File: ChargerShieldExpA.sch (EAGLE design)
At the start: 99 parts, among them IC1 LM324N, IC2 TL431, Q1 BD648, Q2 BUZ11, Q3 BUZ171, Q4 IRFZ48Z, T2 BC548, X1 +Vin, X2 Battery, X3 VCC

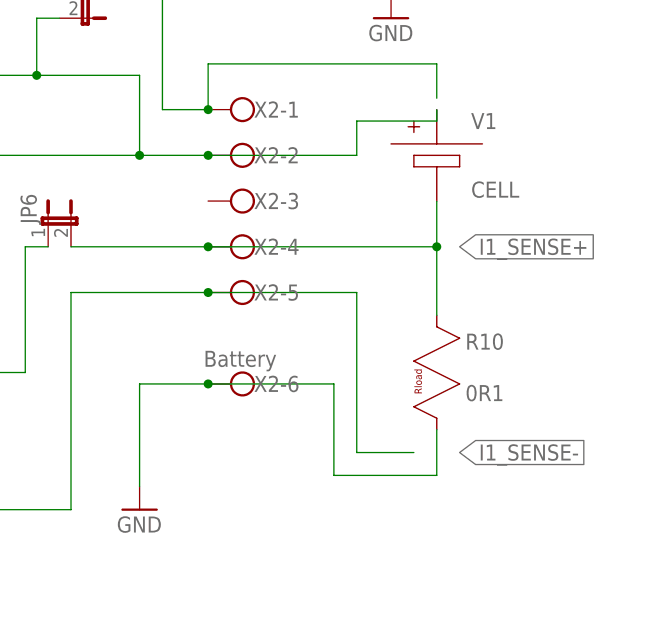
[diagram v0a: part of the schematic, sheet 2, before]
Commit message: internal current sense shunt
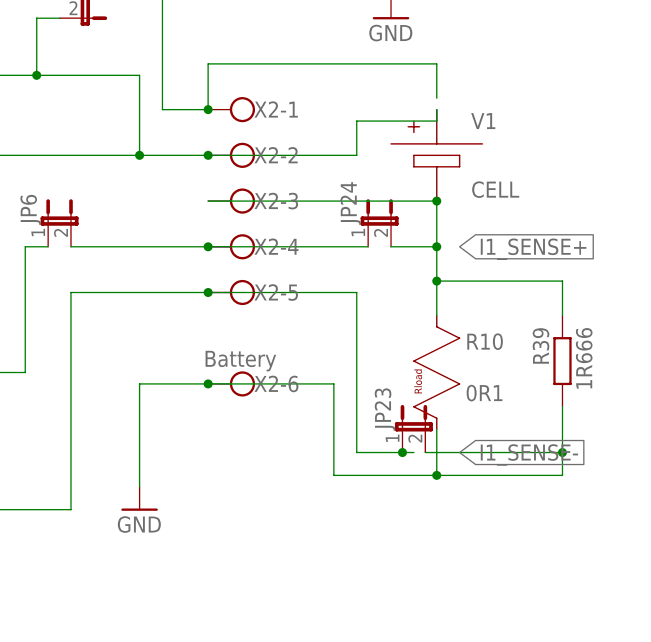
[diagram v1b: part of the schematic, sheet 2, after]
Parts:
- added JP23, JP24: (no value), bigger:JP1E
- added R39: 1R666, rcl:R-EU_0414/15
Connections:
- new net N$54: JP24.1, JP6.2, X2-4.KL
- net GND: now also JP23.2, R39.2
- net I1_SENSE+: now also JP24.2, R39.1, X2-3.KL; no longer JP6.2, X2-4.KL
- net I1_SENSE-: now also JP23.1

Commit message: renumbered
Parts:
- removed C8: 100n, rcl:C-EU025_050-025X075
- removed R39: 1R666, rcl:R-EU_0414/15
- added C7: 10µ, rcl:CPOL-EUE5-5
- added RA10: 0R1, lt-spice-simulation:RES_RLOAD
- C1, C6: value 10µ -> 100n; device rcl:CPOL-EUE5-5 -> rcl:C-EU025_050-025X075
- C4: value 100n -> 3µ3; device rcl:C-EU025_050-025X075 -> rcl:CPOL-EUE5-5
- C5: value 3µ3 -> 10µ
- IC1: value LM324N -> TL431; device linear:LM324N -> AWJLEagleLib:TL431TO92
- IC2: value TL431 -> LM324N; device AWJLEagleLib:TL431TO92 -> linear:LM324N
- JP1, JP2, JP6, JP8: device bigger:JP1E -> bigger:JP2E
- JP16, JP17, JP18, JP9: device bigger:JP2E -> bigger:JP1E
- LED2: value (none) -> CHRG2
- LED3: value CHRG2 -> (none)
- Q1: value BD648 -> BUZ11; device transistor-pnp:BD648 -> transistor-fet:BUZ11
- Q2: value BUZ11 -> BD648; device transistor-fet:BUZ11 -> transistor-pnp:BD648
- R1: value 470 -> 4k7; device rcl:R-EU_0207/12 -> rcl:R-EU_0204/7
- R10: value 0R1 -> 2k2; device lt-spice-simulation:RES_RLOAD -> rcl:R-EU_0207/15
- R11: value 100k -> 1k; device rcl:R-EU_0207/10 -> rcl:R-EU_0204/7
- R12: value 1k -> 1R666; device rcl:R-EU_0207/12 -> rcl:R-EU_0414/15
- R14: value 10k -> 0
- R15: value 100k -> 1k
- R16: value 33k -> 1k
- R17: value 1k -> 12k; device rcl:R-EU_0207/15 -> rcl:R-EU_0207/10
- R18: value 12k -> 100k
- R19: value 1k -> 33k; device rcl:R-EU_0204/7 -> rcl:R-EU_0207/10
- R2: value 100k -> 4k7; device rcl:R-EU_0204/7 -> rcl:R-EU_0207/10
- R20: value 470 -> 1k; device rcl:R-EU_0207/10 -> rcl:R-EU_0207/15
- R21: value 200 -> 1k; device rcl:R-EU_0204/7 -> rcl:R-EU_0207/12
- R22: value 4k7 -> 200; device rcl:R-EU_0207/10 -> rcl:R-EU_0207/12
- R23: value 470 -> 1M
- R24: value 0 -> 100k; device rcl:R-EU_0207/10 -> rcl:R-EU_0204/7
- R25: value 4k7 -> 1k; device rcl:R-EU_0204/7 -> rcl:R-EU_0207/10
- R26: value 470 -> 100k
- R27: value 470 -> 10k; device rcl:R-EU_0204/7 -> rcl:R-EU_0207/10
- R28: value 0 -> 10k; device rcl:R-EU_0204/7 -> rcl:R-EU_0207/10
- R29: value 0 -> 1k; device rcl:R-EU_0204/7 -> rcl:R-EU_0207/12
- R3: device rcl:R-EU_0207/10 -> rcl:R-EU_0207/12
- R30: value 0 -> 100k; device rcl:R-EU_0204/7 -> rcl:R-EU_0207/10
- R31: value 0 -> 1R666; device rcl:R-EU_0204/7 -> rcl:R-EU_0414/15
- R33: device rcl:R-EU_0204/2V -> rcl:R-EU_0204/7
- R34: device rcl:R-EU_0204/7 -> rcl:R-EU_0204/2V
- R35: value 100k -> 0
- R36: value 1M -> 0; device rcl:R-EU_0207/10 -> rcl:R-EU_0204/7
- R37: value 200 -> 0; device rcl:R-EU_0207/12 -> rcl:R-EU_0204/7
- R38: value 1k -> 0; device rcl:R-EU_0207/10 -> rcl:R-EU_0204/7
- R4: value 2k2 -> 200; device rcl:R-EU_0207/15 -> rcl:R-EU_0204/7
- R5, R6: value 1k -> 470
- R7: value 1R666 -> 470; device rcl:R-EU_0414/15 -> rcl:R-EU_0207/10
- R8: value 1k -> 470; device rcl:R-EU_0207/12 -> rcl:R-EU_0204/7
- R9: value 10k -> 470; device rcl:R-EU_0207/10 -> rcl:R-EU_0204/7
- S4: value Discharge -> A
- S5: value A -> B
- S6: value B -> Discharge
- U$1: value ARDUINOR3BPLACE-LONG -> DS1820TO92; device arduino-long:ARDUINOR3BPLACE-LONG -> Ava:DS1820TO92
- U$2: value DS1820TO92 -> ARDUINOR3BPLACE-LONG; device Ava:DS1820TO92 -> arduino-long:ARDUINOR3BPLACE-LONG
- X2: value Battery -> VCC; device con-wago-500:W237-6 -> con-wago-500:W237-102
- X3: value VCC -> Battery; device con-wago-500:W237-102 -> con-wago-500:W237-6
- renumbered T2 to T1
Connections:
- net +5V: now also JP20.1, JP3.1, JP3.2, JP6.3, JP8.3, R1.2, R4.2, U$1.VCC, U$2.5V; no longer JP16.1, JP16.2, JP16.3, JP5.3, JP9.1, R21.2, R25.2, U$1.5V, U$2.VCC
- net GND: now also C1.2, C4.-, C7.-, IC1.A, IC2P.V-, JP17.2, JP2.1, JP2.2, JP2.3, JP20.3, JP4.2, JP6.1, R12.2, R17.1, R19.1, R23.1, R25.1, R26.1, R30.1, R31.2, R32.2, R33.2, R37.2, RA10.B, U$2.GND1, U$2.GND2, X2-2.KL, X3-6.KL; no longer C1.-, C4.2, C6.-, IC1P.V-, IC2.A, JP18.1, JP18.2, JP18.3, JP22.2, JP23.2, JP3.1, JP9.3, R10.B, R11.1, R16.1, R18.1, R28.2, R29.2, R34.2, R35.1, R36.1, R38.1, R39.2, R7.2, U$1.GND1, U$1.GND2, X2-6.KL, X3-2.KL
- net I1_SENSE+: now also JP16.2, R31.1, RA10.A, X3-3.KL; no longer JP24.2, R10.A, R39.1, X2-3.KL
- net I1_SENSE-: now also JP17.1, R28.1, X3-5.KL; no longer JP23.1, R9.1, X2-5.KL
- net I_BATT1: now also C4.+, R21.1, U$2.A1; no longer C2.+, R12.1, U$1.A1
- net I_BATT2: now also JP5.2, U$2.A4/SDA; no longer JP20.2, U$1.A4/SDA
- net I_DISC1: now also R20.2, U$2.A2; no longer R17.2, U$1.A2
- net I_DISC2: now also JP5.3, U$2.A5/SCL; no longer JP20.3, U$1.A5/SCL
- net N$1: now also R3.2, U$2.D13; no longer R1.2, U$1.D13
- net N$10: now also C6.1, JP13.1; no longer C8.1, JP1.1
- net N$11: now also IC2A.OUT, JP12.2, R24.2; no longer IC1A.OUT, JP7.2, R2.2
- net N$12: now also JP6.2, R1.1, U$1.DQ, U$2.D2; no longer JP3.2, R25.1, U$1.D2, U$2.DQ
- net N$13: now also JP13.2, JP15.2, Q1.D, X3-2.KL; no longer JP1.2, JP2.2, Q2.D, X2-2.KL
- net N$14: now also IC2A.-IN, R24.1, R28.2; no longer IC1A.-IN, R2.1, R9.2
- net N$15: now also IC2A.+IN, R26.2, R27.1; no longer IC1A.+IN, R14.1, R35.2
- net N$16: now also IC2B.-IN, R17.2, R18.1, R19.2; no longer IC1B.-IN, R15.1, R16.2, R18.2
- net N$17: now also IC2B.OUT, JP11.1, R18.2; no longer IC1B.OUT, JP15.1, R15.2
- net N$18: now also Q1.G, R11.2; no longer Q2.G, R19.2
- net N$19: now also R5.2, U$2.D5; no longer R3.2, U$1.D5
- net N$2: now also R3.1; no longer R1.1
- net N$20: now also LED3.A, R6.2; no longer LED2.A, R20.2
- net N$21: now also R7.2; no longer R23.2
- net N$22: now also JP14.1, R27.2; no longer JP6.1, R14.2
- net N$23: now also S6.2, U$2.D12; no longer S4.2, U$1.D12
- net N$24: now also LED2.A, R5.1; no longer LED3.A, R3.1
- net N$25: now also JP10.1, Q1.S, R12.1; no longer JP8.1, Q2.S, R7.1
- net N$26: now also U$2.D4; no longer U$1.D4
- net N$27: now also IC1.C, IC1.R, R2.2, R4.1; no longer IC2.C, IC2.R, R21.1, R22.2
- net N$28: now also R2.1, U$2.AREF; no longer R22.1, U$1.AREF
- net N$29: now also C2.+, IC2B.+IN, R14.1; no longer C5.+, IC1B.+IN, R24.1
- net N$3: now also C7.+, JP18.1, R29.2, R30.2; no longer C1.+, JP4.1, R13.2, R8.2
- net N$30: now also U$2.D7; no longer U$1.D7
- net N$31: now also U$2.D8; no longer U$1.D8
- net N$32: now also JP12.1, R21.2; no longer JP7.1, R12.2
- net N$33: now also JP10.2, R14.2; no longer JP8.2, R24.2
- net N$34: now also IC2C.OUT, JP21.1, R34.1; no longer IC1C.OUT, JP11.1, R33.1
- net N$35: now also JP11.2, R20.1; no longer JP15.2, R17.1
- net N$36: now also IC2D.-IN, R36.1, R37.1; no longer IC1D.-IN, R29.1, R31.1
- net N$37: now also S4.2, U$2.D6; no longer S5.2, U$1.D6
- net N$38: now also S5.2, U$2.SDA; no longer S6.2, U$1.SDA
- net N$39: now also R8.2; no longer R26.2
- net N$4: now also C1.1, IC2P.V+, JP8.2; no longer C4.1, IC1P.V+, JP5.2
- net N$40: now also R9.2; no longer R27.2
- net N$41: now also R9.1, U$2.SCL; no longer R27.1, U$1.SCL
- net N$42: now also JP7.2, R8.1, U$2.D1; no longer JP21.2, R26.1, U$1.D1
- net N$43: now also IC2C.+IN, JP19.2; no longer IC1C.+IN, JP10.2
- net N$44: now also JP19.1, R32.1; no longer JP10.1, R28.1
- net N$45: now also IC2D.+IN, R35.1, R38.2; no longer IC1D.+IN, R30.1, R32.2
- net N$46: now also JP22.1, JP22.2, R35.2; no longer JP12.1, JP12.2, R30.2
- net N$47: now also JP23.1, JP23.2, R36.2; no longer JP13.1, JP13.2, R31.2
- net N$48: now also IC2D.OUT, JP24.1, JP24.2, R38.1; no longer IC1D.OUT, JP14.1, JP14.2, R32.1
- net N$49: now also IC2C.-IN, R33.1, R34.2; no longer IC1C.-IN, R33.2, R34.1
- net N$5: now also R10.2, R13.2; no longer R11.2, R4.2
- net N$50: now also C6.2, R25.2; no longer C8.2, R38.2
- net N$51: now also R22.2, R23.2; no longer R36.2, R37.2
- net N$52: now also JP7.1, U$2.D0; no longer JP21.1, U$1.D0
- net N$53: now also JP4.1, U$2./RESET; no longer JP22.1, U$1./RESET
- net N$54: now also JP14.2, JP16.1, X3-4.KL; no longer JP24.1, JP6.2, X2-4.KL
- net N$6: now also R15.1; no longer R5.1
- net N$7: now also Q2.B, R15.2, R16.1; no longer Q1.B, R5.2, R6.1
- net N$8: now also JP15.1, R29.1, X3-1.KL; no longer JP2.1, R8.1, X2-1.KL
- net N$9: now also Q2.C; no longer Q1.C
- net PWM_CHARGE1: now also R10.1, U$2.D3; no longer R4.1, U$1.D3
- net PWM_CHARGE2: now also R22.1, U$2.D11; no longer R37.1, U$1.D11
- net PWM_DISCHARGE1: now also R11.1, R6.1, U$2.D10; no longer R19.1, R20.1, U$1.D10
- net PWM_DISCHARGE2: now also R7.1, U$2.D9; no longer R23.1, U$1.D9
- net U_BATT1: now also JP18.2, U$2.A0; no longer JP4.2, U$1.A0
- net U_BATT2: now also JP5.1, U$2.A3; no longer JP20.1, U$1.A3
- net VCC: now also C5.+, JP20.2, JP8.1, JP9.1, Q2.E, R16.2, X2-1.KL; no longer C6.+, JP19.1, JP5.1, JP9.2, Q1.E, R6.2, X3-1.KL
- net VIN: now also JP1.1, JP1.2, JP1.3, JP9.2, U$2.VIN; no longer JP17.1, JP17.2, JP17.3, JP19.2, U$1.VIN

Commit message: before production
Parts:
- added R39: *, rcl:R-EU_0204/7
- R21: device rcl:R-EU_0207/12 -> rcl:R-EU_0204/7
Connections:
- net GND: now also R39.1
- net N$32: now also R39.2
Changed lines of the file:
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@@
 <grid distance="0.05" unitdist="inch" unit="mm" style="lines" multiple="1" display="yes" altdistance="0.025" altunitdist="inch" altunit="mm"/>
 <layers>
-<layer number="1" name="Top" color="4" fill="1" visible="no" active="no"/>
-<layer number="2" name="Route2" color="1" fill="3" visible="no" active="no"/>
-<layer number="3" name="Route3" color="4" fill="3" visible="no" active="no"/>
-<layer number="4" name="Route4" color="1" fill="4" visible="no" active="no"/>
-<layer number="5" name="Route5" color="4" fill="4" visible="no" active="no"/>
-<layer number="6" name="Route6" color="1" fill="8" visible="no" active="no"/>
-<layer number="7" name="Route7" color="4" fill="8" visible="no" active="no"/>
-<layer number="8" name="Route8" color="1" fill="2" visible="no" active="no"/>
-<layer number="9" name="Route9" color="4" fill="2" visible="no" active="no"/>
-<layer number="10" name="Route10" color="1" fill="7" visible="no" active="no"/>
-<layer number="11" name="Route11" color="4" fill="7" visible="no" active="no"/>
-<layer number="12" name="Route12" color="1" fill="5" visible="no" active="no"/>
-<layer number="13" name="Route13" color="4" fill="5" visible="no" active="no"/>
-<layer number="14" name="Route14" color="1" fill="6" visible="no" active="no"/>
-<layer number="15" name="Route15" color="4" fill="6" visible="no" active="no"/>
-<layer number="16" name="Bottom" color="1" fill="1" visible="no" active="no"/>
-<layer number="17" name="Pads" color="2" fill="1" visible="no" active="no"/>
-<layer number="18" name="Vias" color="2" fill="1" visible="no" active="no"/>
-<layer number="19" name="Unrouted" color="6" fill="1" visible="no" active="no"/>
-<layer number="20" name="Dimension" color="15" fill="1" visible="no" active="no"/>
-<layer number="21" name="tPlace" color="7" fill="1" visible="no" active="no"/>
-<layer number="22" name="bPlace" color="7" fill="1" visible="no" active="no"/>
-<layer number="23" name="tOrigins" color="15" fill="1" visible="no" active="no"/>
-<layer number="24" name="bOrigins" color="15" fill="1" visible="no" active="no"/>
-<layer number="25" name="tNames" color="7" fill="1" visible="no" active="no"/>
-<layer number="26" name="bNames" color="7" fill="1" visible="no" active="no"/>
-<layer number="27" name="tValues" color="7" fill="1" visible="no" active="no"/>
-<layer number="28" name="bValues" color="7" fill="1" visible="no" active="no"/>
+<layer number="1" name="Top" color="4" fill="1" visible="yes" active="no"/>
+<layer number="2" name="Route2" color="1" fill="3" visible="yes" active="no"/>
+<layer number="3" name="Route3" color="4" fill="3" visible="yes" active="no"/>
+<layer number="4" name="Route4" color="1" fill="4" visible="yes" active="no"/>
+<layer number="5" name="Route5" color="4" fill="4" visible="yes" active="no"/>
+<layer number="6" name="Route6" color="1" fill="8" visible="yes" active="no"/>
+<layer number="7" name="Route7" color="4" fill="8" visible="yes" active="no"/>
+<layer number="8" name="Route8" color="1" fill="2" visible="yes" active="no"/>
+<layer number="9" name="Route9" color="4" fill="2" visible="yes" active="no"/>
+<layer number="10" name="Route10" color="1" fill="7" visible="yes" active="no"/>
+<layer number="11" name="Route11" color="4" fill="7" visible="yes" active="no"/>
+<layer number="12" name="Route12" color="1" fill="5" visible="yes" active="no"/>
+<layer number="13" name="Route13" color="4" fill="5" visible="yes" active="no"/>
+<layer number="14" name="Route14" color="1" fill="6" visible="yes" active="no"/>
+<layer number="15" name="Route15" color="4" fill="6" visible="yes" active="no"/>
+<layer number="16" name="Bottom" color="1" fill="1" visible="yes" active="no"/>
+<layer number="17" name="Pads" color="2" fill="1" visible="yes" active="no"/>
+<layer number="18" name="Vias" color="2" fill="1" visible="yes" active="no"/>
+<layer number="19" name="Unrouted" color="6" fill="1" visible="yes" active="no"/>
+<layer number="20" name="Dimension" color="15" fill="1" visible="yes" active="no"/>
+<layer number="21" name="tPlace" color="7" fill="1" visible="yes" active="no"/>
+<layer number="22" name="bPlace" color="7" fill="1" visible="yes" active="no"/>
+<layer number="23" name="tOrigins" color="15" fill="1" visible="yes" active="no"/>
+<layer number="24" name="bOrigins" color="15" fill="1" visible="yes" active="no"/>
+<layer number="25" name="tNames" color="7" fill="1" visible="yes" active="no"/>
+<layer number="26" name="bNames" color="7" fill="1" visible="yes" active="no"/>
+<layer number="27" name="tValues" color="7" fill="1" visible="yes" active="no"/>
+<layer number="28" name="bValues" color="7" fill="1" visible="yes" active="no"/>
 <layer number="29" name="tStop" color="7" fill="3" visible="no" active="no"/>
 <layer number="30" name="bStop" color="7" fill="6" visible="no" active="no"/>
@@
 <layer number="35" name="tGlue" color="7" fill="4" visible="no" active="no"/>
 <layer number="36" name="bGlue" color="7" fill="5" visible="no" active="no"/>
-<layer number="37" name="tTest" color="7" fill="1" visible="no" active="no"/>
-<layer number="38" name="bTest" color="7" fill="1" visible="no" active="no"/>
+<layer number="37" name="tTest" color="7" fill="1" visible="yes" active="no"/>
+<layer number="38" name="bTest" color="7" fill="1" visible="yes" active="no"/>
 <layer number="39" name="tKeepout" color="4" fill="11" visible="no" active="no"/>
 <layer number="40" name="bKeepout" color="1" fill="11" visible="no" active="no"/>
@@
 <layer number="44" name="Drills" color="7" fill="1" visible="no" active="no"/>
 <layer number="45" name="Holes" color="7" fill="1" visible="no" active="no"/>
-<layer number="46" name="Milling" color="3" fill="1" visible="no" active="no"/>
-<layer number="47" name="Measures" color="7" fill="1" visible="no" active="no"/>
-<layer number="48" name="Document" color="7" fill="1" visible="no" active="no"/>
-<layer number="49" name="Reference" color="7" fill="1" visible="no" active="no"/>
-<layer number="50" name="dxf" color="7" fill="1" visible="no" active="no"/>
-<layer number="51" name="tDocu" color="7" fill="1" visible="no" active="no"/>
-<layer number="52" name="bDocu" color="7" fill="1" visible="no" active="no"/>
-<layer number="53" name="tGND_GNDA" color="7" fill="9" visible="no" active="no"/>
-<layer number="54" name="bGND_GNDA" color="1" fill="9" visible="no" active="no"/>
-<layer number="56" name="wert" color="7" fill="1" visible="no" active="no"/>
-<layer number="57" name="tCAD" color="7" fill="1" visible="no" active="no"/>
+<layer number="46" name="Milling" color="3" fill="1" visible="yes" active="no"/>
+<layer number="47" name="Measures" color="7" fill="1" visible="yes" active="no"/>
+<layer number="48" name="Document" color="7" fill="1" visible="yes" active="no"/>
+<layer number="49" name="Reference" color="7" fill="1" visible="yes" active="no"/>
+<layer number="50" name="dxf" color="7" fill="1" visible="yes" active="no"/>
+<layer number="51" name="tDocu" color="7" fill="1" visible="yes" active="no"/>
+<layer number="52" name="bDocu" color="7" fill="1" visible="yes" active="no"/>
+<layer number="53" name="tGND_GNDA" color="7" fill="9" visible="yes" active="no"/>
+<layer number="54" name="bGND_GNDA" color="1" fill="9" visible="yes" active="no"/>
+<layer number="56" name="wert" color="7" fill="1" visible="yes" active="no"/>
+<layer number="57" name="tCAD" color="7" fill="1" visible="yes" active="no"/>
 <layer number="91" name="Nets" color="2" fill="1" visible="yes" active="yes"/>
 <layer number="92" name="Busses" color="1" fill="1" visible="yes" active="yes"/>
@@
 <part name="GND10" library="supply1" deviceset="GND" device=""/>
 <part name="R13" library="rcl" deviceset="R-EU_" device="0207/10" value="100k"/>
-<part name="R21" library="rcl" deviceset="R-EU_" device="0207/12" value="1k"/>
+<part name="R21" library="rcl" deviceset="R-EU_" device="0204/7" value="1k"/>
 <part name="R30" library="rcl" deviceset="R-EU_" device="0207/10" value="100k"/>
 <part name="C7" library="rcl" deviceset="CPOL-EU" device="E5-5" value="10µ"/>
@@
 <part name="JP17" library="bigger" deviceset="JP1E" device=""/>
 <part name="JP16" library="bigger" deviceset="JP1E" device=""/>
+<part name="R39" library="rcl" deviceset="R-EU_" device="0204/7" value="*"/>
 </parts>
 <sheets>
@@
 <instance part="JP17" gate="A" x="240.03" y="77.47"/>
 <instance part="JP16" gate="A" x="236.22" y="100.33"/>
+<instance part="R39" gate="G$1" x="134.62" y="72.39" rot="R90"/>
 </instances>
 <busses>
@@
 <pinref part="C4" gate="G$1" pin="-"/>
 <pinref part="GND5" gate="1" pin="GND"/>
-<wire x1="120.65" y1="68.58" x2="120.65" y2="66.04" width="0.1524" layer="91"/>
+<wire x1="120.65" y1="68.58" x2="120.65" y2="67.31" width="0.1524" layer="91"/>
+<pinref part="R39" gate="G$1" pin="1"/>
+<wire x1="120.65" y1="67.31" x2="120.65" y2="66.04" width="0.1524" layer="91"/>
+<wire x1="134.62" y1="67.31" x2="120.65" y2="67.31" width="0.1524" layer="91"/>
+<junction x="120.65" y="67.31"/>
 </segment>
 <segment>
@@
 <pinref part="R21" gate="G$1" pin="2"/>
 <pinref part="JP12" gate="A" pin="1"/>
-<wire x1="139.7" y1="81.28" x2="132.08" y2="81.28" width="0.1524" layer="91"/>
-</segment>
-</net>
+<wire x1="139.7" y1="81.28" x2="134.62" y2="81.28" width="0.1524" layer="91"/>
+<pinref part="R39" gate="G$1" pin="2"/>
+<wire x1="134.62" y1="81.28" x2="132.08" y2="81.28" width="0.1524" layer="91"/>
+<wire x1="134.62" y1="77.47" x2="134.62" y2="81.28" width="0.1524" layer="91"/>
+<junction x="134.62" y="81.28"/>
+</segment>
+</net>

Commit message: rearranged, better DRC
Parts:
- R35: device rcl:R-EU_0204/7 -> rcl:R-EU_0207/10
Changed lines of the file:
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@@
 <part name="R37" library="rcl" deviceset="R-EU_" device="0204/7" value="0"/>
 <part name="GND15" library="supply1" deviceset="GND" device=""/>
-<part name="R35" library="rcl" deviceset="R-EU_" device="0204/7" value="0"/>
+<part name="R35" library="rcl" deviceset="R-EU_" device="0207/10" value="0"/>
 <part name="R36" library="rcl" deviceset="R-EU_" device="0204/7" value="0"/>
 <part name="R38" library="rcl" deviceset="R-EU_" device="0204/7" value="0"/>
